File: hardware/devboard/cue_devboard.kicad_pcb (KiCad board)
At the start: 4 copper layers, 38 x 28 mm, 56 parts, among them J1 USB-C (power), J2 BATT, J3 LRA, J4 SWD, J5 EXP, SW1 USER, SW2 SHIP/WAKE, U1 BL54L15u, U2 nPM1300, U3 LSM6DSV16BX, U4 T5838, U5 DRV2605L

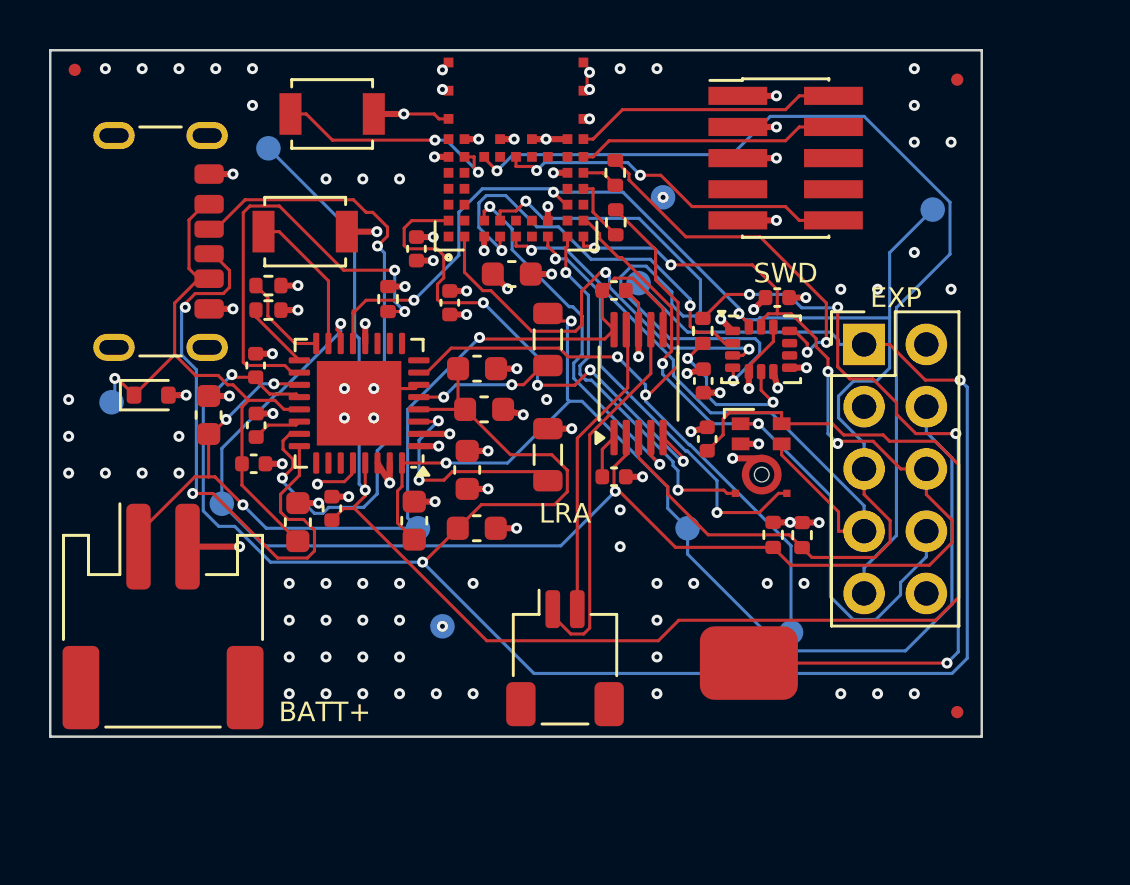
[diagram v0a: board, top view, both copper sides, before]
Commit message: Dev board: regulator layout per Nordic guide; full footprint review
Independent footprint/pin-map review against manufacturer drawings for all
parts found no errors. Layout review against nPM1300 PS 9.3.4 / Fig. 62-65:
- SW1/SW2: hand-routed 2.5 mm, 0.3 mm wide, no vias (was 6-9 mm at 0.127 mm
  through 2 vias each); L1/L2 2.3 mm from the pins, output caps at the
  inductor outputs, PVDD cap 1.5 mm from pin 4.
- Exposed pad: 3x3 GND vias (was 2x2), matching Nordic's reference.
- Power tracks widened after routing where clearance allows (0.2-0.4 mm).
- Escape lane for the LSM6DSV16BX 1V8 pin; cleanup loop routes anything a
  stub removal leaves open. DRC: 0 errors, 0 unconnected.
- J2/U5 footprints re-homed in Cue.pretty with project-local 3D models.
- README: review results, firmware requirements, optional rev B items.

Co-Authored-By: Claude Opus 5.5 <noreply@anthropic.com>
Claude-Session: https://claude.ai/code/session_01DUSU7jbUyc6QVB5XjyAbxC
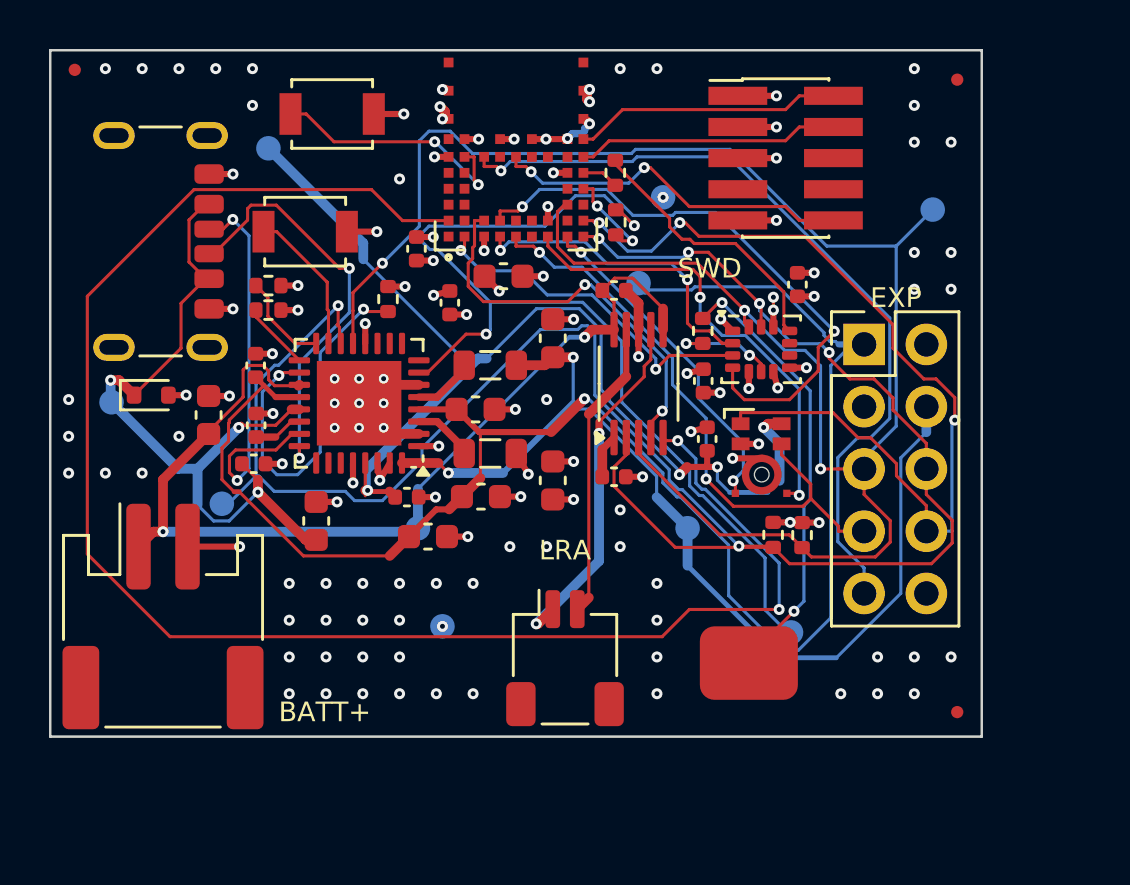
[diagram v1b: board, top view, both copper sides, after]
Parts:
- J2: footprint Connector_JST:JST_PH_S2B-PH-SM4-TB_1x02-1MP_P2.00mm_Horizontal -> Cue:JST_PH_S2B-PH-SM4-TB_1x02-1MP_P2.00mm_Horizontal
- U5: footprint Package_SO:VSSOP-10_3x3mm_P0.5mm -> Cue:VSSOP-10_3x3mm_P0.5mm
- moved C7 9.34 mm to (20.5, 11.8)
- moved C20 5.22 mm to (17.6, 18.2)
- moved C6 3.52 mm to (20.5, 17.6)
- moved C19 3.09 mm to (14.6, 18.2), turned to 0 degrees
- moved L2 2.57 mm to (17.9, 12.8), turned to 0 degrees
- moved L1 2.35 mm to (17.9, 16.4), turned to 0 degrees
- moved C21 2.02 mm to (15.4, 19.8)
- moved C8 0.98 mm to (30.5, 9.56), turned to 90 degrees
- moved C2 0.75 mm to (10.8, 19.2)
- moved C18 0.35 mm to (18.5, 9.22)
- moved C5 0.35 mm to (17.4, 14.7)
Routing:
- net HAPTIC_EN: track 21.6 -> 67.0 mm, vias 4 -> 2
- net I2C_SDA: track 60.0 -> 80.6 mm
- net MIC_1V8: track 64.2 -> 44.8 mm, vias 1 -> 4
- net VSYS: track 86.5 -> 67.6 mm, vias 3 -> 1
- net TOUCH_E: track 32.5 -> 18.3 mm, vias 4 -> 2
- net I2C_SCL: track 70.5 -> 83.1 mm
- net CC1: track 27.1 -> 16.6 mm
- net PDM_DIN: track 28.5 -> 37.1 mm, vias 2 -> 3
- net PMIC_INT: track 32.1 -> 40.7 mm
- net CC2: track 23.7 -> 17.0 mm
- net SW1: track 9.11 -> 2.51 mm, vias 2 -> 0
- net VBUS: track 24.8 -> 31.1 mm, vias 1 -> 3
- net EXP_P0_01: track 39.0 -> 32.8 mm
- net 3V0: track 46.0 -> 40.9 mm
- net TDM_BCLK: track 18.2 -> 14.2 mm
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
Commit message: Dev board: switch radio to Ezurio BL54L15 453-00044 (in stock), 42 x 32 mm
The BL54L15u (453-00223) is out of stock until ~Dec 2026. The dev board now uses
the larger BL54L15 with an MHF4 antenna connector:
- new 39-pad footprint from the Ezurio BL54L10/BL54L15 land pattern, 3D model
- same nRF54L15 port pins as the cuff (firmware unchanged), new pad numbers
- board 42 x 32 mm, re-placed and re-routed: DRC 0 violations, 0 unconnected,
  board = circuit pad for pad
- BOM: U1 453-00044C (global sourcing), J1 -> C5246813 (USB4125-GF-A-0190)
- READMEs: antenna to buy, ordering notes

Co-Authored-By: Claude Opus 5.5 <noreply@anthropic.com>
Claude-Session: https://claude.ai/code/session_01DUSU7jbUyc6QVB5XjyAbxC
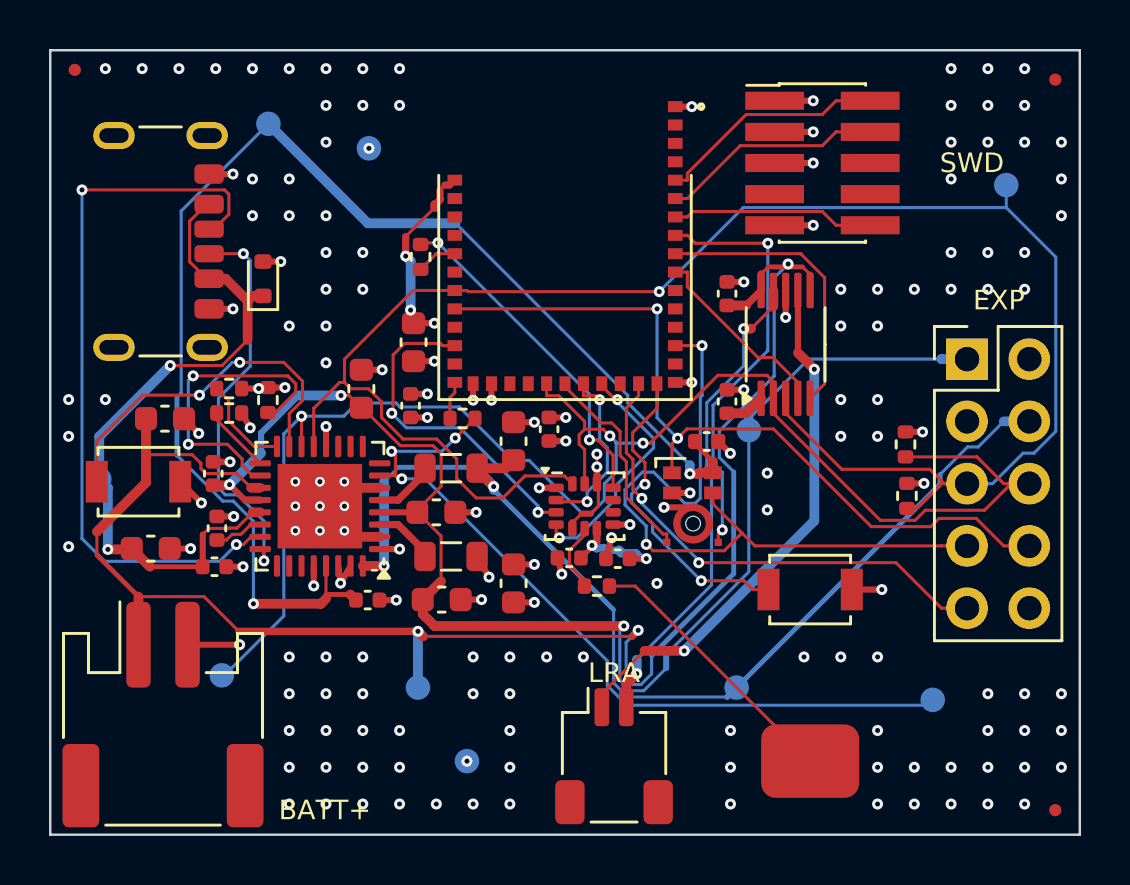
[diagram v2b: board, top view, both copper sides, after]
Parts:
- U1: value BL54L15u -> BL54L15; footprint Cue:Ezurio_BL54L15u_453-00223 -> Cue:Ezurio_BL54L15_453-00044
- moved SW1 27.5 mm to (31.0, 22.0)
- moved C8 13.4 mm to (23.1, 20.7), turned to 0 degrees
- moved SW2 12.3 mm to (3.60, 17.6)
- moved TP4 12.2 mm to (13.0, 4.00)
- moved R6 11.3 mm to (22.3, 21.9), turned to 0 degrees
- moved R8 10.2 mm to (16.8, 15.0), turned to 0 degrees
- moved U3 9.63 mm to (21.8, 18.6)
- moved C16 9.13 mm to (20.4, 15.5)
- moved C9 9.06 mm to (21.2, 20.7), turned to 0 degrees
- moved R7 8.65 mm to (15.1, 8.43)
- moved TP3 7.50 mm to (28.5, 15.5)
- moved TP10 7.00 mm to (7.00, 25.5)
- moved C2 6.84 mm to (4.10, 20.3), turned to 0 degrees
- moved TP5 6.80 mm to (28.0, 26.0)
- moved C21 6.62 mm to (12.7, 13.8), turned to 90 degrees
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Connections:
- U1 pad 1: (no net) -> GND
- U1 pad 10: (no net) -> HAPTIC_TRIG
- U1 pad 13: MIC_THSEL -> (no net)
- U1 pad 14: GND -> PDM_CLK
- U1 pad 15: MIC_WAKE -> (no net)
- U1 pad 16: (no net) -> GND
- U1 pad 17: I2C_SCL -> BTN_USER
- U1 pad 18: PDM_DIN -> EXP_P0_01
- U1 pad 2: HAPTIC_EN -> (no net)
- U1 pad 20: I2C_SDA -> IMU_INT1
- U1 pad 21: U1_PMIC_INT -> TDM_DIN
- U1 pad 22: (no net) -> MIC_WAKE
- U1 pad 23: U1_TDM_WCLK -> I2C_SCL
- U1 pad 24: GND -> (no net)
- U1 pad 25: SWDCLK -> (no net)
- U1 pad 26: (no net) -> 1V8
- U1 pad 27: SWDIO -> GND
- U1 pad 28: GND -> U1_PMIC_INT
- U1 pad 3: TDM_BCLK -> (no net)
- U1 pad 30: (no net) -> TDM_BCLK
- U1 pad 31: GND -> (no net)
- U1 pad 32: nRESET -> PDM_DIN
- U1 pad 33: (no net) -> I2C_SDA
- U1 pad 34: GND -> (no net)
- U1 pad 35: EXP_P0_01 -> U1_TDM_WCLK
- U1 pad 36: GND -> (no net)
- U1 pad 38: BTN_USER -> (no net)
- U1 pad 4: GND -> (no net)
- U1 pad 5: 1V8 -> SWDIO
- U1 pad 6: HAPTIC_TRIG -> SWDCLK
- U1 pad 7: TDM_DIN -> nRESET
- U1 pad 8: IMU_INT1 -> MIC_THSEL
- U1 pad 9: PDM_CLK -> HAPTIC_EN
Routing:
- net HAPTIC_EN: track 67.0 -> 11.7 mm, vias 2 -> 0
- net VBAT: track 40.8 -> 67.9 mm, vias 2 -> 3
- net I2C_SCL: track 83.1 -> 63.8 mm, vias 6 -> 3
- net IMU_INT1: track 23.8 -> 9.82 mm
- net CC1: track 16.6 -> 30.2 mm
- net EXP_P0_01: track 32.8 -> 20.4 mm, vias 1 -> 2
- net VSYS: track 67.6 -> 57.6 mm, vias 1 -> 3
- net MIC_1V8: track 44.8 -> 54.4 mm, vias 4 -> 2
- net HAPTIC_TRIG: track 16.5 -> 7.87 mm, vias 2 -> 0
- net SHPHLD: track 5.97 -> 14.6 mm, vias 0 -> 2
- net PMIC_INT: track 40.7 -> 32.1 mm, vias 2 -> 3
- net I2C_SDA: track 80.6 -> 72.9 mm, vias 3 -> 1
- net LRA_N: track 12.2 -> 19.8 mm, vias 0 -> 2
- net TOUCH_E: track 18.3 -> 11.1 mm, vias 2 -> 0
- net LRA_P: track 14.9 -> 21.8 mm
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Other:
- board size 38 x 28 mm -> 42 x 32 mm
